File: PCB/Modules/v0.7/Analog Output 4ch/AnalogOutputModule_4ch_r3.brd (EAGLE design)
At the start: 85 x 85 mm, 40 parts, among them IC1 SN65HVD31DR, IC2 SN65HVD31DR, IC3 AD5754RBREZ, IC4 REF193GSZ

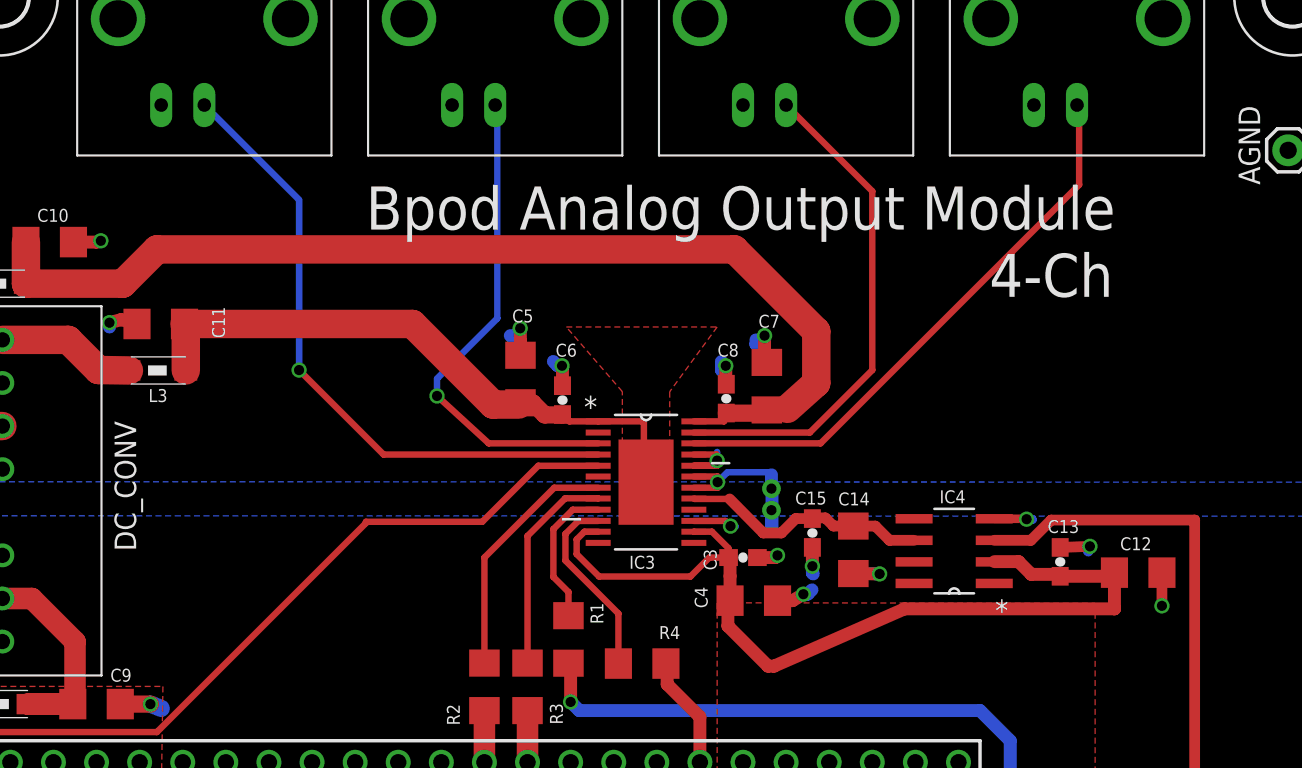
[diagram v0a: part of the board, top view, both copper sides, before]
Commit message: -Updated analog output module PCB design
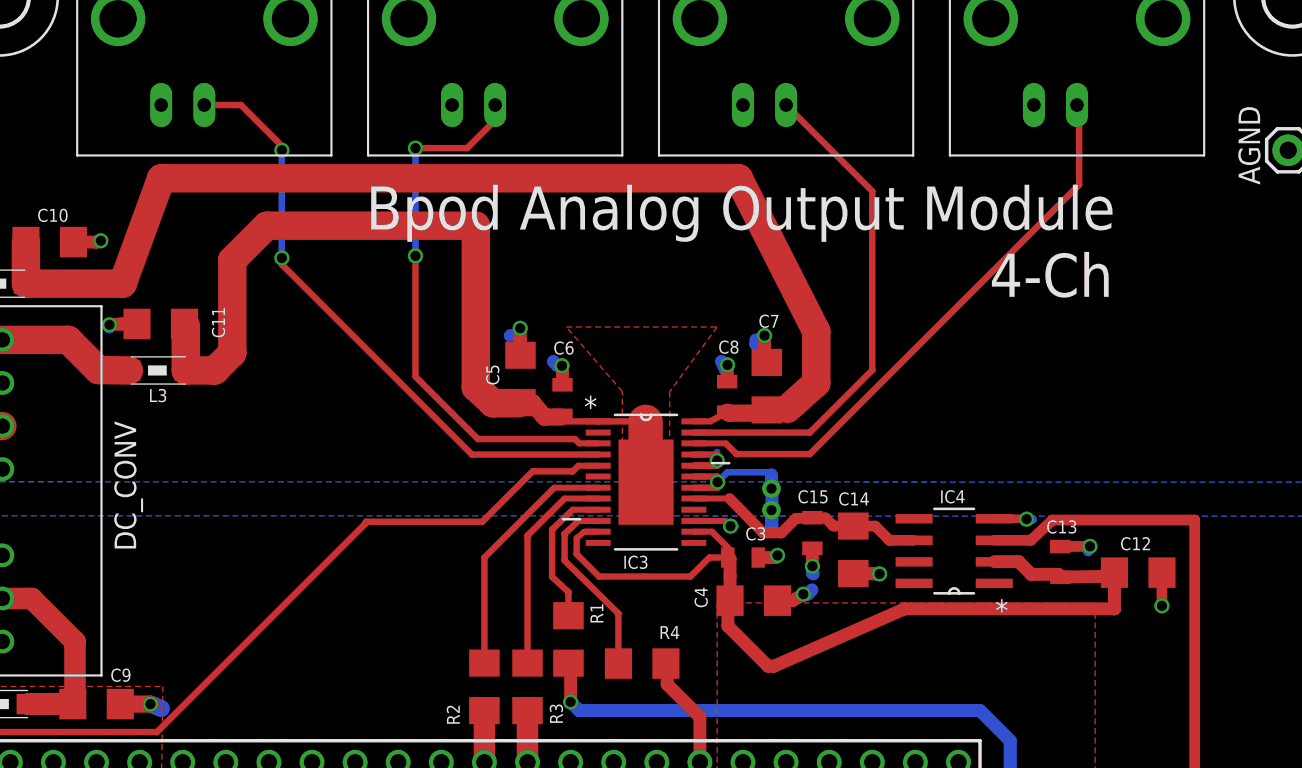
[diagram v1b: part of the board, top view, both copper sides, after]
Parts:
- C1, C10, C11, C12, C14, C2, C4, C5, C7, C9: device SparkFun-Capacitors:1206 -> SparkFun-Capacitors:1206@1
- C13, C15, C3, C6, C8: value 0.1uf -> 0.1uF; device SparkFun-Capacitors:0603-CAP -> SparkFun-Capacitors:0805
- moved C8 0.11 mm to (47.3, 57.1)
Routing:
- net VSS: track 38.1 -> 54.8 mm
- net N$39: track 63.3 -> 70.1 mm
- net N$9: track 29.3 -> 32.1 mm, vias 1 -> 2
- net N$10: track 37.6 -> 35.8 mm, vias 1 -> 2
- net N$12: track 33.8 -> 34.3 mm
